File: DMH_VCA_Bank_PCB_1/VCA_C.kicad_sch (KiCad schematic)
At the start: 22 parts, among them Q5 BC548, Q6 BC548, U2 TL074, U3 TL074

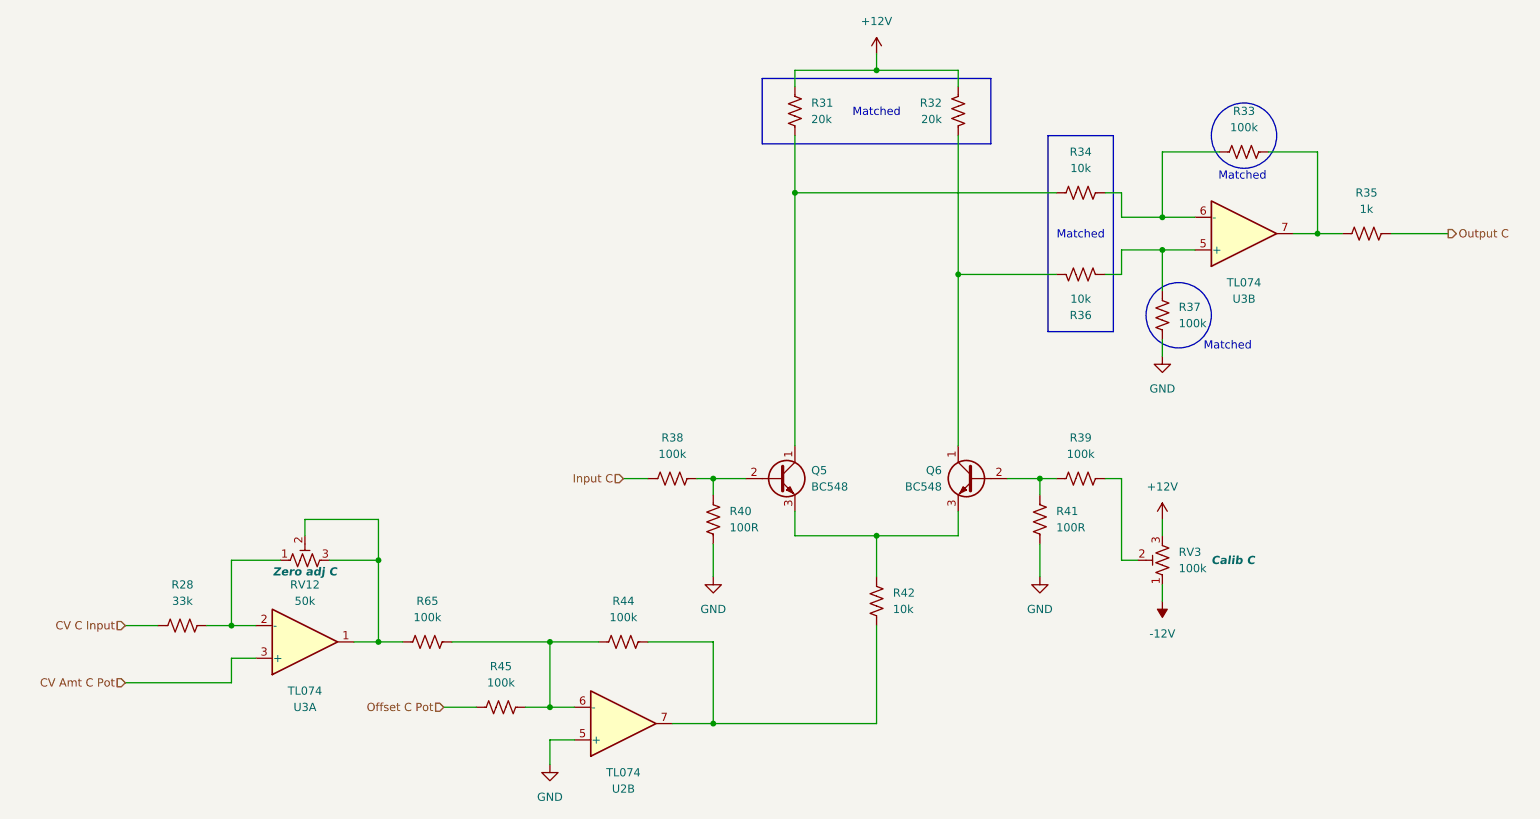
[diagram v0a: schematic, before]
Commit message: Finished schematic of PCB 1
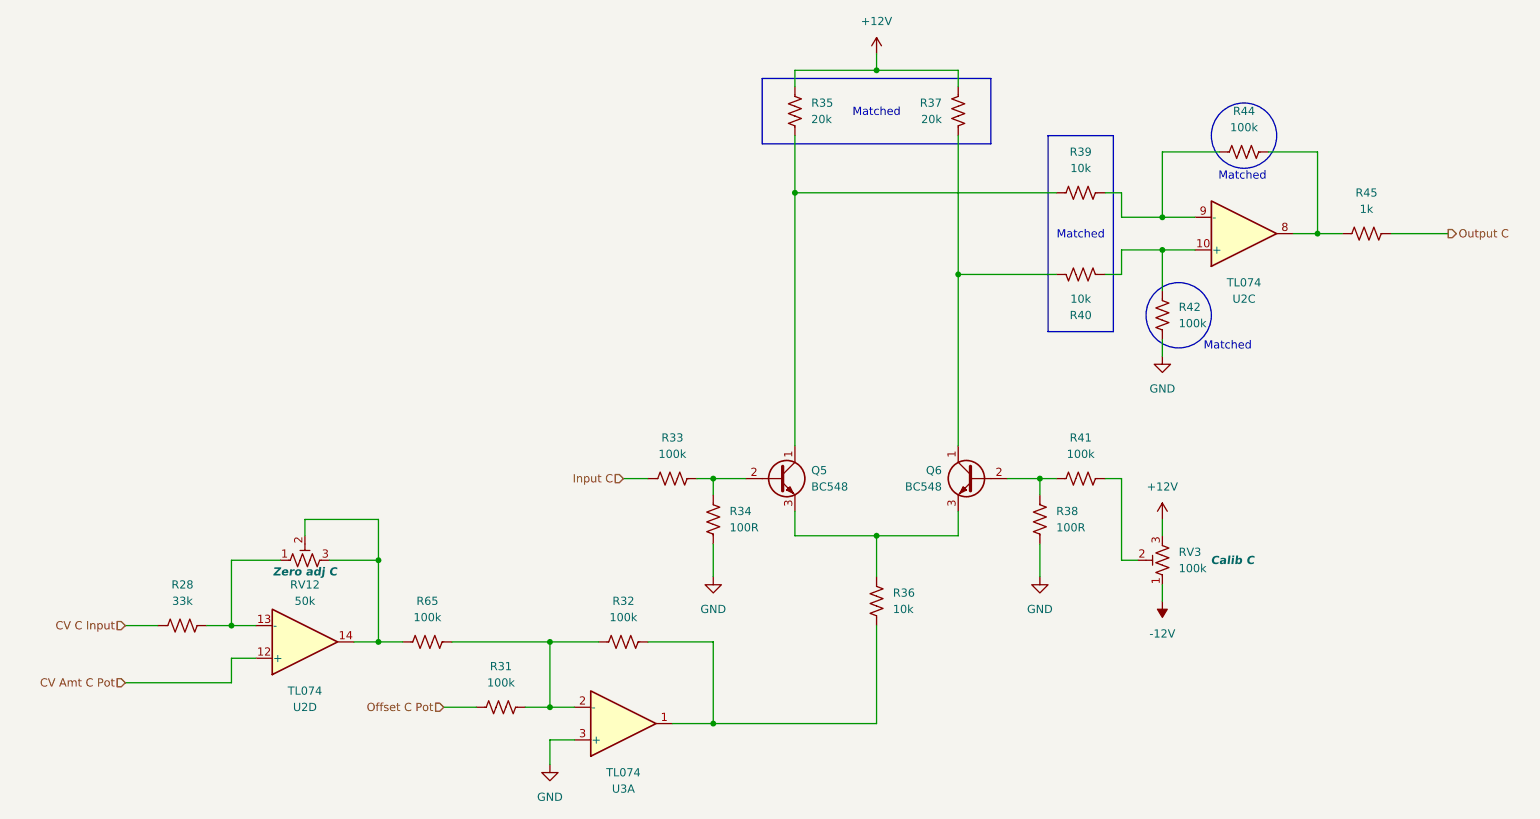
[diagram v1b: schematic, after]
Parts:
- removed U2: TL074, Package_DIP:DIP-14_W7.62mm_Socket, symbol Amplifier_Operational:TL074
- removed unit 2 of U3
- added U2: TL074, Package_DIP:DIP-14_W7.62mm_Socket, symbol Amplifier_Operational:TL074
- R31, R32: value 20k -> 100k
- R34: value 10k -> 100R
- R35: value 1k -> 20k
- R37: value 100k -> 20k
- R38: value 100k -> 100R
- R39: value 100k -> 10k
- R40: value 100R -> 10k
- R41: value 100R -> 100k
- R42: value 10k -> 100k
- R45: value 100k -> 1k
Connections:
- net +12V: now also R35.2, R37.2; no longer R31.2, R32.2
- net CV Amt C Pot: now also U2.12 (+); no longer U3.3 (+)
- net GND: now also R34.1, R38.1, R42.2, U3.3 (+); no longer R37.2, R40.1, R41.1
- net Input C: now also R33.2; no longer R38.2
- net Offset C Pot: now also R31.1; no longer R45.1
- net Output C: now also R45.1; no longer R35.1
- net at R33.1: now also Q5.2 (B), R34.2; no longer R35.2
- net at Q6.2 (B), R41.2: now also R38.2; no longer R39.2
- net at R65.1, RV12.2, RV12.3: now also U2.14; no longer U3.1
- net at R28.2, RV12.1: now also U2.13 (-); no longer U3.2 (-)
- net at R37.1: now also Q6.1 (C), R40.2; no longer R36.1
- net at R44.1, R45.2: now also U2.8; no longer R65.2
- net at R44.2: now also R39.1, U2.9 (-); no longer R42.1
- net at Q5.3 (E), Q6.3 (E): now also R36.2; no longer R42.2
- net at RV3.2: now also R41.1; no longer R39.1
- new net: R31.2, R32.1, R65.2, U3.2 (-)
- new net: R32.2, R36.1, U3.1
- new net: Q5.1 (C), R35.1, R39.2
- new net: R40.1, R42.1, U2.10 (+)
